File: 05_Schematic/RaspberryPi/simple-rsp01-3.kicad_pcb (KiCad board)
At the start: 2 copper layers, 58.4 x 78.7 mm, 21 parts, among them J1 Conn_01x10, J2 Conn_01x02, J3 Conn_01x02, Q1 2N5401L-B-T92-K, Q2 2N5401L-B-T92-K, Q3 DMG3415U, Q4 Q_NMOS_GDS, SW1 SW_SPDT, U1 INA219, U2 DRV8830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

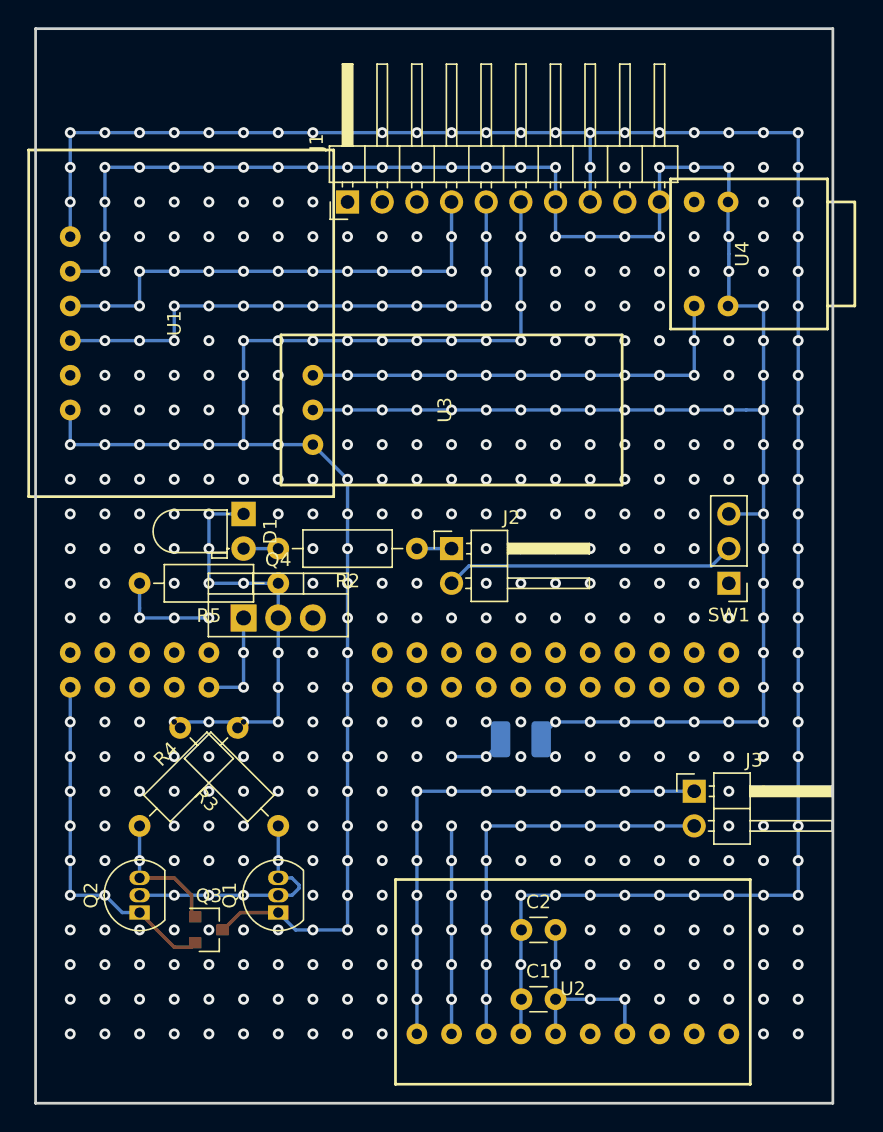
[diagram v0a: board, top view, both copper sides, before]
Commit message: M系基板の回路図の更新
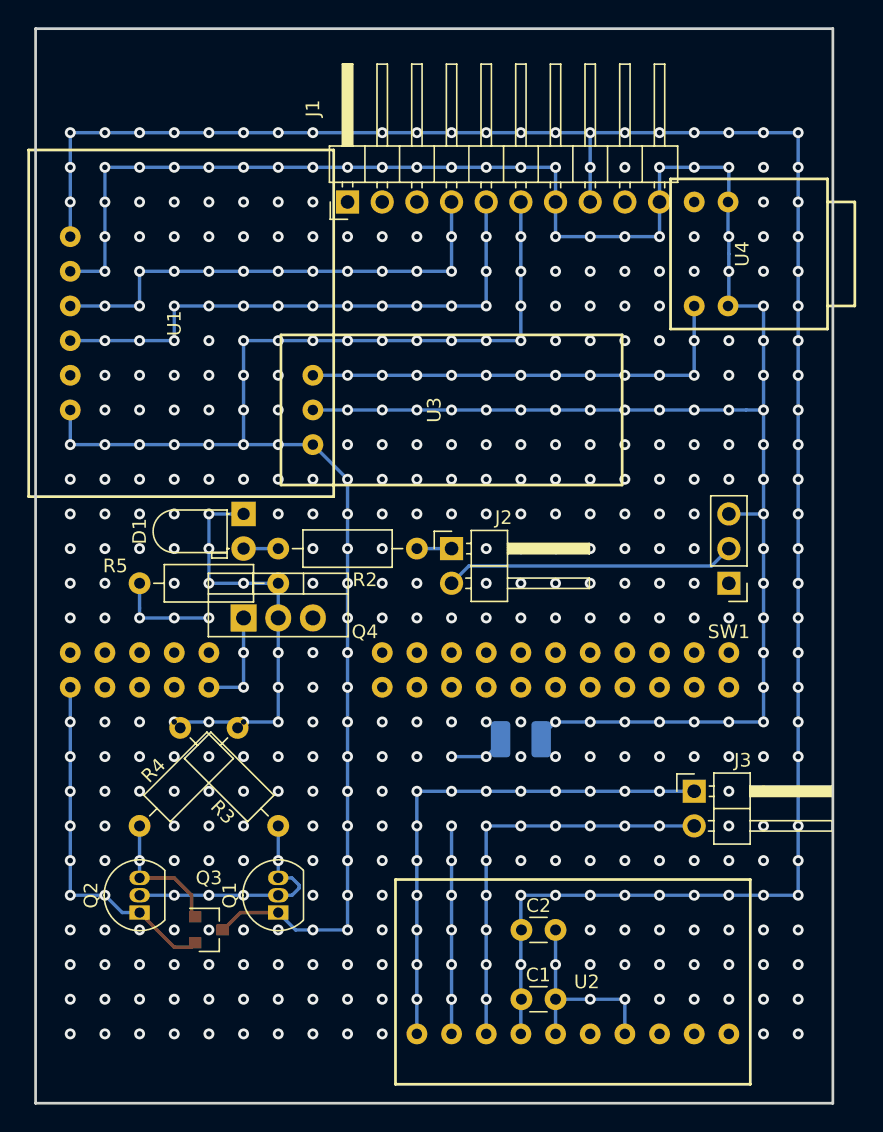
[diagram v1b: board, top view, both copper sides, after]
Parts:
- Q4: value Q_NMOS_GDS -> MTB30N06I3
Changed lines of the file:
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@@
     (at 140.97 115.57)
     (attr through_hole)
-    (fp_text reference "U2" (at 0 0.5) (layer "F.SilkS")
+    (fp_text reference "U2" (at 1.016 0) (layer "F.SilkS")
       (effects (font (size 1 1) (thickness 0.2)))
     )
@@
     (at 132.08 73.66 -90)
     (attr through_hole)
-    (fp_text reference "U3" (at 0 0.5 -90) (layer "F.SilkS")
+    (fp_text reference "U3" (at 0 1.27 -90) (layer "F.SilkS")
       (effects (font (size 1 1) (thickness 0.2)))
     )
@@
     (tags "Through hole angled pin header THT 1x02 2.54mm single row")
     (attr through_hole)
-    (fp_text reference "J2" (at 4.385 -2.27) (layer "F.SilkS")
+    (fp_text reference "J2" (at 3.81 -2.27) (layer "F.SilkS")
       (effects (font (size 1 1) (thickness 0.15)))
     )
@@
     (tags "Through hole pin header THT 1x03 2.54mm single row")
     (attr through_hole)
-    (fp_text reference "SW1" (at 0 -2.33 180) (layer "F.SilkS")
+    (fp_text reference "SW1" (at 0 -3.556 180) (layer "F.SilkS")
       (effects (font (size 1 1) (thickness 0.15)))
     )
@@
     (tags "Resistor Axial_DIN0207 series Axial Horizontal pin pitch 10.16mm 0.25W = 1/4W length 6.3mm diameter 2.5mm")
     (attr through_hole)
-    (fp_text reference "R5" (at 5.08 -2.37 180) (layer "F.SilkS")
+    (fp_text reference "R5" (at 11.938 1.27 180) (layer "F.SilkS")
       (effects (font (size 1 1) (thickness 0.15)))
     )
@@
     (tags "SOT-23")
     (attr smd)
-    (fp_text reference "Q3" (at 0 -2.5) (layer "F.SilkS")
+    (fp_text reference "Q3" (at 0 -3.81) (layer "F.SilkS")
       (effects (font (size 1 1) (thickness 0.15)))
     )
@@
     (tags "TO-220-3 Vertical RM 2.54mm")
     (attr through_hole)
-    (fp_text reference "Q4" (at 2.54 -4.27) (layer "F.SilkS")
-      (effects (font (size 1 1) (thickness 0.15)))
-    )
-    (fp_text value "Q_NMOS_GDS" (at 2.54 2.5) (layer "F.Fab")
+    (fp_text reference "Q4" (at 8.89 1.016) (layer "F.SilkS")
+      (effects (font (size 1 1) (thickness 0.15)))
+    )
+    (fp_text value "MTB30N06I3" (at -7.62 1.016) (layer "F.Fab")
       (effects (font (size 1 1) (thickness 0.15)))
     )
@@
     (tags "Through hole angled pin header THT 1x10 2.54mm single row")
     (attr through_hole)
-    (fp_text reference "J1" (at 4.385 -2.27 90) (layer "F.SilkS")
+    (fp_text reference "J1" (at 6.858 -2.54 90) (layer "F.SilkS")
       (effects (font (size 1 1) (thickness 0.15)))
     )
@@
     (tags "Through hole angled pin header THT 1x02 2.54mm single row")
     (attr through_hole)
-    (fp_text reference "J3" (at 4.385 -2.27) (layer "F.SilkS")
+    (fp_text reference "J3" (at 3.556 -2.27) (layer "F.SilkS")
       (effects (font (size 1 1) (thickness 0.15)))
     )
@@
     (tags "C Disc series Radial pin pitch 2.50mm  diameter 3.0mm width 1.6mm Capacitor")
     (attr through_hole)
-    (fp_text reference "C1" (at 1.25 -2.05) (layer "F.SilkS")
+    (fp_text reference "C1" (at 1.23 -1.778) (layer "F.SilkS")
       (effects (font (size 1 1) (thickness 0.15)))
     )
@@
     (tags "Resistor Axial_DIN0207 series Axial Horizontal pin pitch 10.16mm 0.25W = 1/4W length 6.3mm diameter 2.5mm")
     (attr through_hole)
-    (fp_text reference "R2" (at 5.08 -2.37 180) (layer "F.SilkS")
+    (fp_text reference "R2" (at 3.81 -2.286 180) (layer "F.SilkS")
       (effects (font (size 1 1) (thickness 0.15)))
     )
@@
     (tags "Resistor Axial_DIN0207 series Axial Horizontal pin pitch 10.16mm 0.25W = 1/4W length 6.3mm diameter 2.5mm")
     (attr through_hole)
-    (fp_text reference "R3" (at 5.08 -2.37 135) (layer "F.SilkS")
+    (fp_text reference "R3" (at 3.592102 -2.155261 135) (layer "F.SilkS")
       (effects (font (size 1 1) (thickness 0.15)))
     )
@@
     (tags "Resistor Axial_DIN0207 series Axial Horizontal pin pitch 10.16mm 0.25W = 1/4W length 6.3mm diameter 2.5mm")
     (attr through_hole)
-    (fp_text reference "R4" (at 5.08 -2.37 45) (layer "F.SilkS")
+    (fp_text reference "R4" (at 3.592102 -2.155261 45) (layer "F.SilkS")
       (effects (font (size 1 1) (thickness 0.15)))
     )
@@
     (tags "LED diameter 3.0mm z-position of LED center 2.0mm 2 pins")
     (attr through_hole)
-    (fp_text reference "D1" (at 1.27 -1.96 -90) (layer "F.SilkS")
+    (fp_text reference "D1" (at 1.27 7.62 -90) (layer "F.SilkS")
       (effects (font (size 1 1) (thickness 0.15)))
     )
@@
     (tags "C Disc series Radial pin pitch 2.50mm  diameter 3.0mm width 1.6mm Capacitor")
     (attr through_hole)
-    (fp_text reference "C2" (at 1.25 -2.05) (layer "F.SilkS")
-      (effects (font (size 1 1) (thickness 0.15)))
-    )
+    (fp_text reference "C2" (at 1.25 -1.778) (layer "F.SilkS")
+      (effects (font (size 1 1) (thickness 0.15)))
+    )

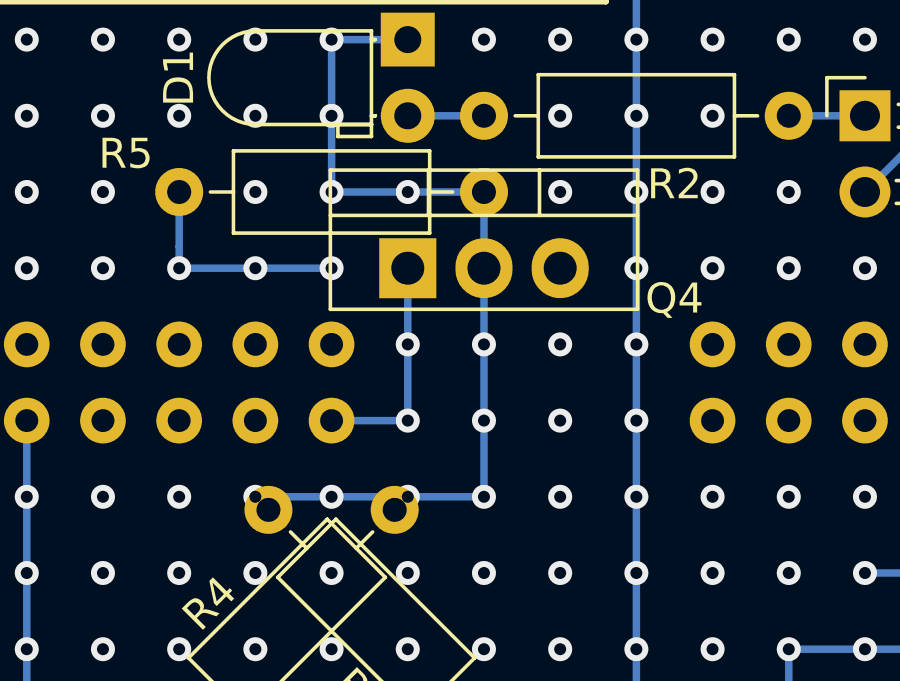
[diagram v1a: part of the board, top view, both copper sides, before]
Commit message: Mission基板FET配線誤りの修正
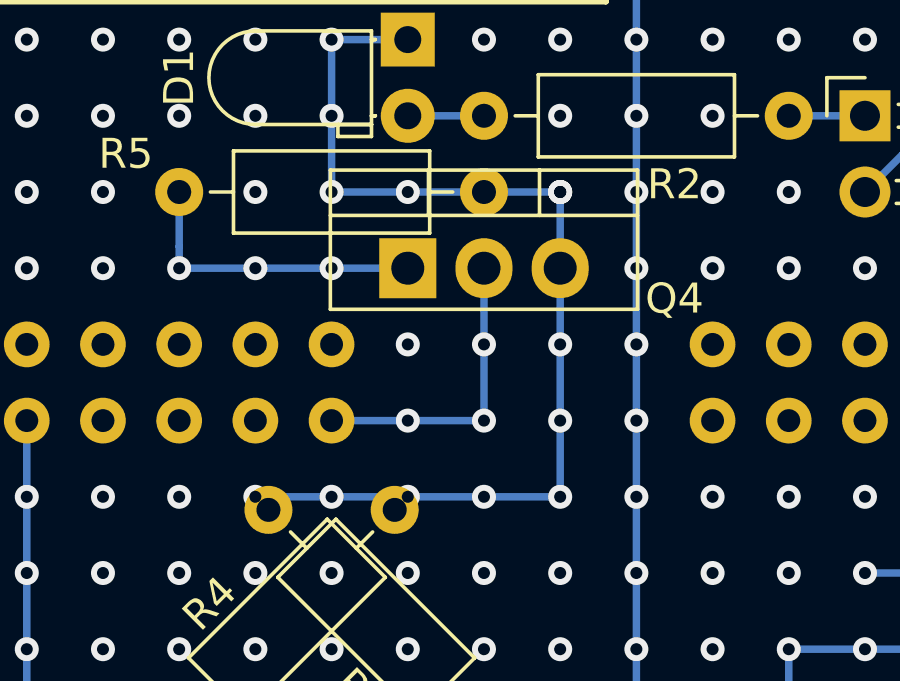
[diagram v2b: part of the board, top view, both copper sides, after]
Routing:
- net GND: track 207.6 -> 212.7 mm, vias 86 -> 87
- net Raspy_Pwrctl: track 7.62 -> 10.2 mm, vias 5 -> 6
- net Net-(Q4-Pad2): track 7.62 -> 10.2 mm, vias 4 -> 5
- net (no net): vias 279 -> 276
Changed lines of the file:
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@@
   (via (at 144.78 83.82) (size 0.8) (drill 0.4) (layers "F.Cu" "B.Cu") (net 0))
   (via (at 121.92 99.06) (size 0.8) (drill 0.4) (layers "F.Cu" "B.Cu") (net 0))
-  (via (at 121.92 93.98) (size 0.8) (drill 0.4) (layers "F.Cu" "B.Cu") (net 0))
   (via (at 129.54 93.98) (size 0.8) (drill 0.4) (layers "F.Cu" "B.Cu") (net 0))
   (via (at 106.68 93.98) (size 0.8) (drill 0.4) (layers "F.Cu" "B.Cu") (net 0))
@@
   (via (at 149.86 81.28) (size 0.8) (drill 0.4) (layers "F.Cu" "B.Cu") (net 0))
   (via (at 109.22 91.44) (size 0.8) (drill 0.4) (layers "F.Cu" "B.Cu") (net 0))
-  (via (at 121.92 91.44) (size 0.8) (drill 0.4) (layers "F.Cu" "B.Cu") (net 0))
   (via (at 137.16 91.44) (size 0.8) (drill 0.4) (layers "F.Cu" "B.Cu") (net 0))
   (via (at 104.14 91.44) (size 0.8) (drill 0.4) (layers "F.Cu" "B.Cu") (net 0))
@@
   (via (at 106.68 96.52) (size 0.8) (drill 0.4) (layers "F.Cu" "B.Cu") (net 0))
   (via (at 132.08 81.28) (size 0.8) (drill 0.4) (layers "F.Cu" "B.Cu") (net 0))
+  (via (at 116.84 91.44) (size 0.8) (drill 0.4) (layers "F.Cu" "B.Cu") (free) (net 0))
   (via (at 142.24 81.28) (size 0.8) (drill 0.4) (layers "F.Cu" "B.Cu") (net 0))
   (via (at 129.54 91.44) (size 0.8) (drill 0.4) (layers "F.Cu" "B.Cu") (net 0))
@@
   (via (at 106.68 81.28) (size 0.8) (drill 0.4) (layers "F.Cu" "B.Cu") (net 0))
   (via (at 132.08 91.44) (size 0.8) (drill 0.4) (layers "F.Cu" "B.Cu") (net 0))
-  (via (at 121.92 96.52) (size 0.8) (drill 0.4) (layers "F.Cu" "B.Cu") (net 0))
   (via (at 134.62 91.44) (size 0.8) (drill 0.4) (layers "F.Cu" "B.Cu") (net 0))
   (via (at 147.32 81.28) (size 0.8) (drill 0.4) (layers "F.Cu" "B.Cu") (net 0))
@@
   (via (at 139.7 86.36) (size 0.8) (drill 0.4) (layers "F.Cu" "B.Cu") (net 0))
   (via (at 129.54 86.36) (size 0.8) (drill 0.4) (layers "F.Cu" "B.Cu") (net 0))
-  (via (at 121.92 86.36) (size 0.8) (drill 0.4) (layers "F.Cu" "B.Cu") (net 0))
   (via (at 127 88.9) (size 0.8) (drill 0.4) (layers "F.Cu" "B.Cu") (net 0))
   (via (at 147.32 88.9) (size 0.8) (drill 0.4) (layers "F.Cu" "B.Cu") (net 0))
@@
   (via (at 154.94 83.82) (size 0.8) (drill 0.4) (layers "F.Cu" "B.Cu") (net 10))
   (via (at 139.7 99.06) (size 0.8) (drill 0.4) (layers "F.Cu" "B.Cu") (net 10))
+  (via (at 121.92 93.98) (size 0.8) (drill 0.4) (layers "F.Cu" "B.Cu") (net 10))
   (via (at 152.4 81.28) (size 0.8) (drill 0.4) (layers "F.Cu" "B.Cu") (net 10))
   (via (at 154.94 81.28) (size 0.8) (drill 0.4) (layers "F.Cu" "B.Cu") (net 10))
-  (via (at 119.38 91.44) (size 0.8) (drill 0.4) (layers "F.Cu" "B.Cu") (net 10))
+  (via (at 121.92 91.44) (size 0.8) (drill 0.4) (layers "F.Cu" "B.Cu") (net 10))
   (via (at 147.32 96.52) (size 0.8) (drill 0.4) (layers "F.Cu" "B.Cu") (net 10))
   (via (at 152.4 96.52) (size 0.8) (drill 0.4) (layers "F.Cu" "B.Cu") (net 10))
@@
   (via (at 114.3 81.28) (size 0.8) (drill 0.4) (layers "F.Cu" "B.Cu") (net 10))
   (via (at 116.84 81.28) (size 0.8) (drill 0.4) (layers "F.Cu" "B.Cu") (net 10))
+  (via (at 121.92 96.52) (size 0.8) (drill 0.4) (layers "F.Cu" "B.Cu") (net 10))
   (via (at 114.3 96.52) (size 0.8) (drill 0.4) (layers "F.Cu" "B.Cu") (net 10))
+  (via (at 121.92 86.36) (size 0.8) (drill 0.4) (layers "F.Cu" "B.Cu") (net 10))
   (via (at 154.94 86.36) (size 0.8) (drill 0.4) (layers "F.Cu" "B.Cu") (net 10))
-  (via (at 119.38 86.36) (size 0.8) (drill 0.4) (layers "F.Cu" "B.Cu") (net 10))
+  (via (at 121.92 86.36) (size 0.8) (drill 0.4) (layers "F.Cu" "B.Cu") (net 10))
   (via (at 154.94 88.9) (size 0.8) (drill 0.4) (layers "F.Cu" "B.Cu") (net 10))
   (via (at 121.92 88.9) (size 0.8) (drill 0.4) (layers "F.Cu" "B.Cu") (net 10))
@@
   (via (at 111.76 96.52) (size 0.8) (drill 0.4) (layers "F.Cu" "B.Cu") (net 10))
   (via (at 149.86 96.52) (size 0.8) (drill 0.4) (layers "F.Cu" "B.Cu") (net 10))
-  (via (at 119.38 88.9) (size 0.8) (drill 0.4) (layers "F.Cu" "B.Cu") (net 10))
   (via (at 142.24 96.52) (size 0.8) (drill 0.4) (layers "F.Cu" "B.Cu") (net 10))
   (via (at 139.7 96.52) (size 0.8) (drill 0.4) (layers "F.Cu" "B.Cu") (net 10))
@@
   (via (at 154.94 93.98) (size 0.8) (drill 0.4) (layers "F.Cu" "B.Cu") (net 10))
   (via (at 114.3 86.36) (size 0.8) (drill 0.4) (layers "F.Cu" "B.Cu") (net 10))
-  (via (at 119.38 93.98) (size 0.8) (drill 0.4) (layers "F.Cu" "B.Cu") (net 10))
   (via (at 154.94 91.44) (size 0.8) (drill 0.4) (layers "F.Cu" "B.Cu") (net 10))
   (via (at 139.7 111.76) (size 0.8) (drill 0.4) (layers "F.Cu" "B.Cu") (net 10))
@@
   (via (at 144.78 119.38) (size 0.8) (drill 0.4) (layers "F.Cu" "B.Cu") (net 10))
   (segment (start 147.32 58.42) (end 147.32 55.88) (width 0.25) (layer "B.Cu") (net 10))
+  (segment (start 116.84 86.36) (end 121.92 86.36) (width 0.25) (layer "B.Cu") (net 10))
   (segment (start 152.4 60.96) (end 152.4 62.23) (width 0.25) (layer "B.Cu") (net 10))
   (segment (start 139.7 96.52) (end 138.43 97.79) (width 0.25) (layer "B.Cu") (net 10))
@@
   (segment (start 147.32 55.88) (end 152.4 55.88) (width 0.25) (layer "B.Cu") (net 10))
   (segment (start 154.94 66.04) (end 154.94 96.52) (width 0.25) (layer "B.Cu") (net 10))
-  (segment (start 119.38 86.36) (end 119.38 96.52) (width 0.25) (layer "B.Cu") (net 10))
   (segment (start 106.68 63.5) (end 104.14 63.5) (width 0.25) (layer "B.Cu") (net 10))
+  (segment (start 121.92 86.36) (end 121.92 96.52) (width 0.25) (layer "B.Cu") (net 10))
   (segment (start 139.7 60.96) (end 147.32 60.96) (width 0.25) (layer "B.Cu") (net 10))
   (segment (start 116.84 81.28) (end 114.3 81.28) (width 0.25) (layer "B.Cu") (net 10))
   (segment (start 144.78 116.84) (end 144.78 119.38) (width 0.25) (layer "B.Cu") (net 10))
-  (segment (start 119.38 96.52) (end 116.84 96.52) (width 0.25) (layer "B.Cu") (net 10))
+  (segment (start 121.92 96.52) (end 116.84 96.52) (width 0.25) (layer "B.Cu") (net 10))
   (segment (start 139.7 58.42) (end 139.7 60.96) (width 0.25) (layer "B.Cu") (net 10))
   (segment (start 114.3 86.36) (end 116.84 86.36) (width 0.25) (layer "B.Cu") (net 10))
@@
   (segment (start 152.34 60.9) (end 152.4 60.96) (width 0.25) (layer "B.Cu") (net 10))
   (segment (start 106.68 55.88) (end 106.68 63.5) (width 0.25) (layer "B.Cu") (net 10))
-  (segment (start 116.84 86.36) (end 119.38 86.36) (width 0.25) (layer "B.Cu") (net 10))
   (segment (start 152.4 55.88) (end 152.4 58.42) (width 0.25) (layer "B.Cu") (net 10))
   (segment (start 147.32 58.42) (end 147.32 60.96) (width 0.25) (layer "B.Cu") (net 10))
@@
   (via (at 109.22 88.9) (size 0.8) (drill 0.4) (layers "F.Cu" "B.Cu") (net 22))
   (via (at 109.22 86.36) (size 0.8) (drill 0.4) (layers "F.Cu" "B.Cu") (net 22))
+  (via (at 116.84 88.9) (size 0.8) (drill 0.4) (layers "F.Cu" "B.Cu") (net 22))
   (via (at 111.76 88.9) (size 0.8) (drill 0.4) (layers "F.Cu" "B.Cu") (net 22))
   (via (at 114.3 88.9) (size 0.8) (drill 0.4) (layers "F.Cu" "B.Cu") (net 22))
@@
   (segment (start 109.22 88.174999) (end 109.22 88.9) (width 0.25) (layer "B.Cu") (net 22))
   (segment (start 109.22 86.36) (end 109.22 88.174999) (width 0.25) (layer "B.Cu") (net 22))
+  (segment (start 114.3 88.9) (end 116.84 88.9) (width 0.25) (layer "B.Cu") (net 22))
   (via (at 116.84 93.98) (size 0.8) (drill 0.4) (layers "F.Cu" "B.Cu") (net 23))
-  (via (at 116.84 91.44) (size 0.8) (drill 0.4) (layers "F.Cu" "B.Cu") (net 23))
-  (via (at 116.84 88.9) (size 0.8) (drill 0.4) (layers "F.Cu" "B.Cu") (net 23))
+  (via (at 119.38 91.44) (size 0.8) (drill 0.4) (layers "F.Cu" "B.Cu") (free) (net 23))
+  (via (at 119.38 88.9) (size 0.8) (drill 0.4) (layers "F.Cu" "B.Cu") (net 23))
+  (via (at 119.38 93.98) (size 0.8) (drill 0.4) (layers "F.Cu" "B.Cu") (free) (net 23))
   (via (at 114.3 93.98) (size 0.8) (drill 0.4) (layers "F.Cu" "B.Cu") (net 23))
-  (segment (start 116.84 91.44) (end 116.84 93.98) (width 0.25) (layer "B.Cu") (net 23))
-  (segment (start 116.84 88.9) (end 116.84 91.44) (width 0.25) (layer "B.Cu") (net 23))
+  (segment (start 116.84 93.98) (end 119.38 93.98) (width 0.25) (layer "B.Cu") (net 23))
+  (segment (start 119.38 88.9) (end 119.38 91.44) (width 0.25) (layer "B.Cu") (net 23))
+  (segment (start 119.38 91.44) (end 119.38 93.98) (width 0.25) (layer "B.Cu") (net 23))
   (segment (start 114.3 93.98) (end 116.84 93.98) (width 0.25) (layer "B.Cu") (net 23))
   (via (at 149.86 58.42) (size 0.8) (drill 0.4) (layers "F.Cu" "B.Cu") (net 24))
